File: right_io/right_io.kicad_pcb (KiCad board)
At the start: 8 copper layers, 58 x 185 mm, 163 parts, among them J11 USB-C dual-role data/PD port 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, J12 USB-C source-only data port J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, J30 External HDMI-A from TCP0, J500 JXD1-1022NL recessed 1GbE RJ45, Q2002 2N7002K DFP USB2 enable inver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, Q50 BSS138 HDMI bias gate, U1760 TPS2553DDBVR 1.3A USB branch, U1761 TPS25810RVCR Type-C DFP contr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, U1763 TPD1S514-1YZR 5.9V VBUS OVP, U1765 TPD4E05U06 USB2/CC ESD, U2011 TPD4S201 CC and USB2 short-to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, U2012 CAT24C256 32KB private TPS257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, U2013 TS3USB30E DFP-qualified USB2 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, U2014 SN74LVC2G07 partial-power-dow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, U2015 TVS2200 22V USB VBUS surge cl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, U2016 SN74LVC1G08 DFP and attached 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, U42 TPS25751AD USB-PD DRP control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, U50 TPD13S523PWR HDMI control ESD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, U500 RTL8111H-CG-RH PCIe Gigabit E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, U501 D3V3XA4B10LP-7 four-channel 0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, U502 D3V3XA4B10LP-7 four-channel 0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, U51 PCA9306DCTR HDMI DDC level tr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, U53 SN74LVC1G17DBVR HDMI HPD buff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, U54 TPS22975NDSGR host-active SYS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, U55 TPS22975NDSGR host-active SYS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, U721 TPS26630RGER PD2 default-off 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, Y500 ECS-250-8-33-AGN-TR 25MHz 8pF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

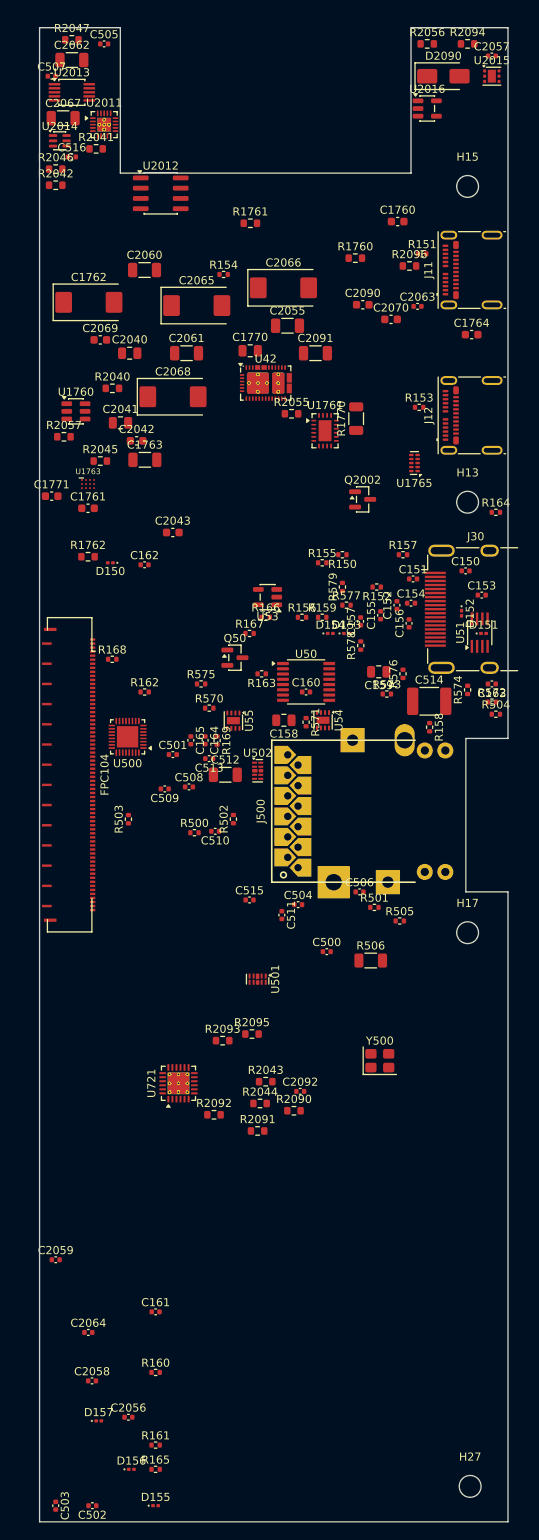
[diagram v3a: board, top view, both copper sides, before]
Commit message: Phase 5: second-opinion audit remediation + rebuilt, verified board pipeline
Second-opinion AI audit found A-tier defects; remediation applied and the
board pipeline rebuilt on a known-good base with the fixes it needed:

- electrical: LTC4418IUF symbol pinout corrected (both selectors were
  dead as drawn); center charge cascade (U15 <- U15B, PD1 > PD2 > AUX);
  pack negative never crosses FPC-3, 15-pin FG_VSS return; power-budgeted
  FPC pin maps (0.4 A/pin derate); J12/DS4 completed; AUX source fuse
- FH41-68S footprint: 13 datasheet-correct SH pads + SH pin in symbol
- connector geometry settled against the Hirose FH12 2D drawing: FFC
  enters opposite the solder pins (mouth = local +Y); reversed side-B
  maps are correct for the 180-deg-mounted pairs; rotations set so mouths
  face across every seam
- pipeline (generate_split_boards.py): per-pin pad-net resync from the
  netlists (kills shadow nets for good), netlist-exact name
  normalization, netlist-only part injection (cascade, probe headers),
  zone refill after outline swap, read-before-write race fixed, orphan
  parts dropped loudly, non-zero exit on unresolved overlaps
- monolith board relocated to old/monolith_ducktop2.kicad_pcb (placement
  oracle for the center cut only)

verified end state: 4 boards 0 shorts / 0 clearance / 0 drill, 0 boundary
crossings, 6/6 connectors contract-exact with mouths facing, 0 shadow
nets, gates PASS x4, ERC 0 x4. routing next (499 nets/board).
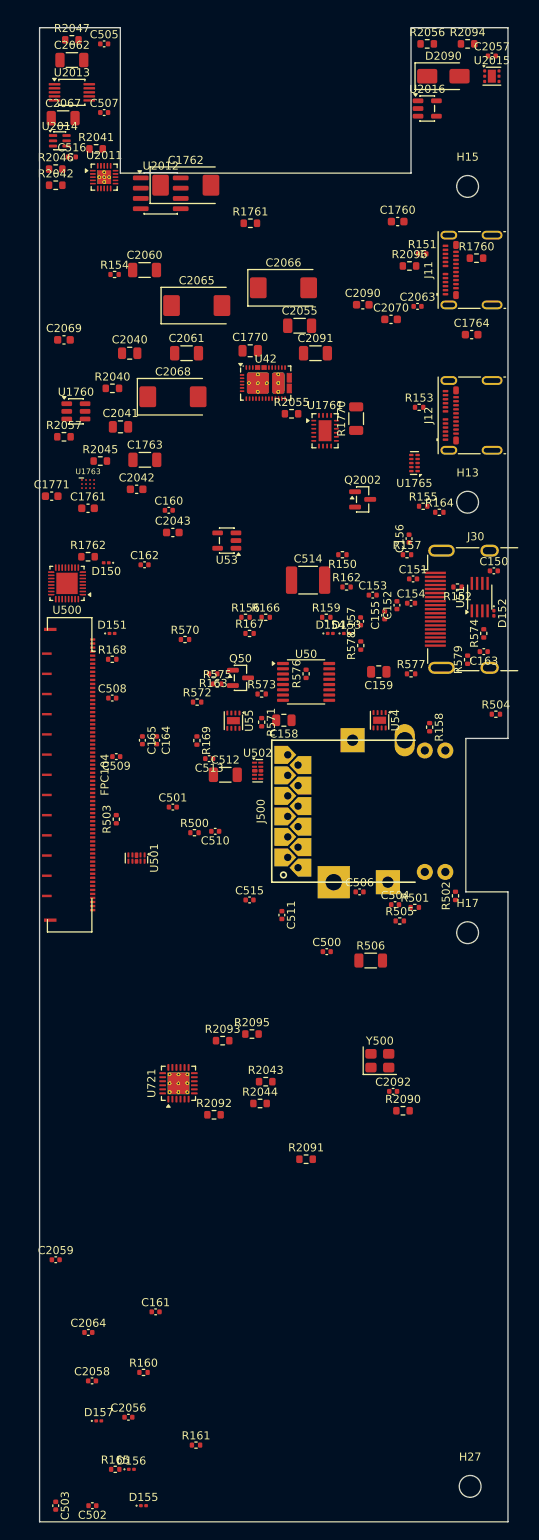
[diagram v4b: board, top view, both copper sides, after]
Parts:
- H13, H15, H17, H27: value MountingHole_2.7mm_M2.5 -> M2.5 isolated mainboard mounting hole
- moved D151 46.0 mm to (309.0, 75.0)
- moved R572 36.5 mm to (319.5, 83.5)
- moved R502 29.1 mm to (351.5, 107.5)
- moved C160 28.2 mm to (316.0, 59.8)
- moved R162 28.2 mm to (338.0, 69.2)
- moved C514 21.2 mm to (333.2, 68.4)
- moved U501 21.2 mm to (312.0, 102.8)
- moved U500 20.4 mm to (303.4, 68.8)
- moved C1762 18.8 mm to (318.1, 19.5)
- moved R579 17.9 mm to (353.0, 78.2)
- moved R573 15.5 mm to (327.5, 82.5)
- moved R1760 15.0 mm to (354.1, 28.5)
- moved C508 14.5 mm to (309.0, 83.0)
- moved R155 14.3 mm to (347.5, 59.2)
- moved C153 13.5 mm to (341.2, 70.2)
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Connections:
- net ETH_1V0 renamed /GbE/ETH_1V0
- net ETH_CHASSIS renamed /GbE/ETH_CHASSIS
- net ETH_CT renamed /GbE/ETH_CT
- net ETH_LED_1000_A renamed /GbE/ETH_LED_1000_A
- net ETH_LED_1000_N renamed /GbE/ETH_LED_1000_N
- net ETH_LED_ACT_A renamed /GbE/ETH_LED_ACT_A
- net ETH_LED_ACT_N renamed /GbE/ETH_LED_ACT_N
- net ETH_MDI0_N renamed /GbE/ETH_MDI0_N
- net ETH_MDI0_P renamed /GbE/ETH_MDI0_P
- net ETH_MDI1_N renamed /GbE/ETH_MDI1_N
- net ETH_MDI1_P renamed /GbE/ETH_MDI1_P
- net ETH_MDI2_N renamed /GbE/ETH_MDI2_N
- net ETH_MDI2_P renamed /GbE/ETH_MDI2_P
- net ETH_MDI3_N renamed /GbE/ETH_MDI3_N
- net ETH_MDI3_P renamed /GbE/ETH_MDI3_P
- net ETH_RSET renamed /GbE/ETH_RSET
- net ETH_XI renamed /GbE/ETH_XI
- net ETH_XO renamed /GbE/ETH_XO
- net EXT_HDMI_5V renamed /HDMI/EXT_HDMI_5V
- net EXT_HDMI_BIAS_GATE renamed /HDMI/EXT_HDMI_BIAS_GATE
- net EXT_HDMI_BIAS_RETURN renamed /HDMI/EXT_HDMI_BIAS_RETURN
- net EXT_HDMI_CK_N renamed /HDMI/EXT_HDMI_CK_N
- net EXT_HDMI_CK_P renamed /HDMI/EXT_HDMI_CK_P
- net EXT_HDMI_D0_N renamed /HDMI/EXT_HDMI_D0_N
- net EXT_HDMI_D0_P renamed /HDMI/EXT_HDMI_D0_P
- net EXT_HDMI_D1_N renamed /HDMI/EXT_HDMI_D1_N
- net EXT_HDMI_D1_P renamed /HDMI/EXT_HDMI_D1_P
- net EXT_HDMI_D2_N renamed /HDMI/EXT_HDMI_D2_N
- net EXT_HDMI_D2_P renamed /HDMI/EXT_HDMI_D2_P
- net EXT_HDMI_HPD_CONN renamed /HDMI/EXT_HDMI_HPD_CONN
- net EXT_HDMI_HPD_NODE renamed /HDMI/EXT_HDMI_HPD_NODE
- net EXT_HDMI_SCL_CONN renamed /HDMI/EXT_HDMI_SCL_CONN
- net EXT_HDMI_SDA_CONN renamed /HDMI/EXT_HDMI_SDA_CONN
- net GBE_HSI_N renamed /GbE/GBE_HSI_N
- net GBE_HSI_P renamed /GbE/GBE_HSI_P
- net GBE_HSO_N renamed /GbE/GBE_HSO_N
- net GBE_HSO_P renamed /GbE/GBE_HSO_P
- net GBE_ISOLATE_N renamed /GbE/GBE_ISOLATE_N
- net HDMI_3V3_SWITCH_CT renamed /HDMI/HDMI_3V3_SWITCH_CT
- net HDMI_5V_SWITCH_CT renamed /HDMI/HDMI_5V_SWITCH_CT
- net HDMI_DDC_REF5 renamed /HDMI/HDMI_DDC_REF5
- net HDMI_HOST_3V3 renamed /HDMI/HDMI_HOST_3V3
- net HDMI_SOURCE_5V renamed /HDMI/HDMI_SOURCE_5V
- net HDMI_TPD_D0_UNUSED renamed /HDMI/HDMI_TPD_D0_UNUSED
- net HDMI_TPD_D1_UNUSED renamed /HDMI/HDMI_TPD_D1_UNUSED
- net HDMI_TPD_D2_UNUSED renamed /HDMI/HDMI_TPD_D2_UNUSED
- net HDMI_TPD_D3_UNUSED renamed /HDMI/HDMI_TPD_D3_UNUSED
- net HDMI_TPD_D4_UNUSED renamed /HDMI/HDMI_TPD_D4_UNUSED
- net HDMI_TPD_D5_UNUSED renamed /HDMI/HDMI_TPD_D5_UNUSED
- net HDMI_TPD_D6_UNUSED renamed /HDMI/HDMI_TPD_D6_UNUSED
- net HDMI_TPD_D7_UNUSED renamed /HDMI/HDMI_TPD_D7_UNUSED
- net HDMI_TPD_D8_UNUSED renamed /HDMI/HDMI_TPD_D8_UNUSED
- net HDMI_TPD_D9_UNUSED renamed /HDMI/HDMI_TPD_D9_UNUSED
- net J12_5V_PRE renamed /PD2 Dual-Role/J12_5V_PRE
- net J12_CC1 renamed /PD2 Dual-Role/J12_CC1
- net J12_CC2 renamed /PD2 Dual-Role/J12_CC2
- net J12_ILIM renamed /PD2 Dual-Role/J12_ILIM
- net J12_POL_N renamed /PD2 Dual-Role/J12_POL_N
- net J12_REF renamed /PD2 Dual-Role/J12_REF
- net J12_REF_RTN renamed /PD2 Dual-Role/J12_REF_RTN
- net J12_VBUS renamed /PD2 Dual-Role/J12_VBUS
- net J12_VBUS_POWER renamed /PD2 Dual-Role/J12_VBUS_POWER
- net J12_VBUS_SYS renamed /PD2 Dual-Role/J12_VBUS_SYS
- net PD2_CC1_CONN renamed /PD2 Dual-Role/PD2_CC1_CONN
- net PD2_CC1_SYS renamed /PD2 Dual-Role/PD2_CC1_SYS
- net PD2_CC2_CONN renamed /PD2 Dual-Role/PD2_CC2_CONN
- net PD2_CC2_SYS renamed /PD2 Dual-Role/PD2_CC2_SYS
- net PD2_CC_ESD_VBIAS renamed /PD2 Dual-Role/PD2_CC_ESD_VBIAS
- net PD2_CC_FAULT_LOCAL_N renamed /PD2 Dual-Role/PD2_CC_FAULT_LOCAL_N
- net PD2_DM_CONN renamed /PD2 Dual-Role/PD2_DM_CONN
- net PD2_DM_HOST_SWITCHED renamed /PD2 Dual-Role/PD2_DM_HOST_SWITCHED
- net PD2_DP_CONN renamed /PD2 Dual-Role/PD2_DP_CONN
- net PD2_DP_HOST_SWITCHED renamed /PD2 Dual-Role/PD2_DP_HOST_SWITCHED
- net PD2_DRAIN_THERMAL renamed /PD2 Dual-Role/PD2_DRAIN_THERMAL
- net PD2_EEPROM_IRQ_N renamed /PD2 Dual-Role/PD2_EEPROM_IRQ_N
- net PD2_EEPROM_SCL renamed /PD2 Dual-Role/PD2_EEPROM_SCL
- net PD2_EEPROM_SDA renamed /PD2 Dual-Role/PD2_EEPROM_SDA
- net PD2_EFUSE_DVDT renamed /PD2 Dual-Role/PD2_EFUSE_DVDT
- net PD2_EFUSE_ILIM renamed /PD2 Dual-Role/PD2_EFUSE_ILIM
- net PD2_EFUSE_OV renamed /PD2 Dual-Role/PD2_EFUSE_OV
- net PD2_EFUSE_SHDN renamed /PD2 Dual-Role/PD2_EFUSE_SHDN
- net PD2_EFUSE_UV renamed /PD2 Dual-Role/PD2_EFUSE_UV
- net PD2_GPIO_ATTACH renamed /PD2 Dual-Role/PD2_GPIO_ATTACH
- net PD2_GPIO_DFP renamed /PD2 Dual-Role/PD2_GPIO_DFP
- net PD2_GPIO_FLIP renamed /PD2 Dual-Role/PD2_GPIO_FLIP
- net PD2_HOST_ATTACHED renamed /PD2 Dual-Role/PD2_HOST_ATTACHED
- net PD2_LDO1V5 renamed /PD2 Dual-Role/PD2_LDO1V5
- net PD2_LDO3V3 renamed /PD2 Dual-Role/PD2_LDO3V3
- net PD2_MUX_EN renamed /PD2 Dual-Role/PD2_MUX_EN
- net PD2_MUX_FLIP renamed /PD2 Dual-Role/PD2_MUX_FLIP
- net PD2_PPHV renamed /PD2 Dual-Role/PD2_PPHV
- net PD2_USB2_OE_N renamed /PD2 Dual-Role/PD2_USB2_OE_N
- C150 pad 1: TCP0_TX0_P -> /TCP0_TX0_P
- C151 pad 1: TCP0_TX0_N -> /TCP0_TX0_N
- C152 pad 1: TCP0_TXRX0_P -> /TCP0_TXRX0_P
- C153 pad 1: TCP0_TXRX0_N -> /TCP0_TXRX0_N
- C154 pad 1: TCP0_TX1_P -> /TCP0_TX1_P
- C155 pad 1: TCP0_TX1_N -> /TCP0_TX1_N
- C156 pad 1: TCP0_TXRX1_P -> /TCP0_TXRX1_P
- C157 pad 1: TCP0_TXRX1_N -> /TCP0_TXRX1_N
- C1760 pad 1: USB_PORT_5V -> /USB_PORT_5V
- C1764 pad 1: SYS_3V3 -> /SYS_3V3
- C2043 pad 1: SYS_3V3 -> /SYS_3V3
- C2055 pad 1: PD2_VBUS_RAW -> /PD2_VBUS_RAW
- C2056 pad 1: PD2_VBUS_RAW -> /PD2_VBUS_RAW
- C2057 pad 1: PD2_VBUS_RAW -> /PD2_VBUS_RAW
- C2058 pad 1: PD2_VBUS_RAW -> /PD2_VBUS_RAW
- C2059 pad 1: PD2_VBUS_RAW -> /PD2_VBUS_RAW
- C2062 pad 1: MCU_3V3 -> /MCU_3V3
- C2065 pad 1: USB_PORT_5V -> /USB_PORT_5V
- C2066 pad 1: USB_PORT_5V -> /USB_PORT_5V
- C2067 pad 1: USB_PORT_5V -> /USB_PORT_5V
- C2070 pad 1: SYS_3V3 -> /SYS_3V3
- C2091 pad 1: PD2_VBUS_GATED -> /PD2_VBUS_GATED
- C500 pad 1: GBE_HOST_TX_P -> /GBE_HOST_TX_P
- C501 pad 1: GBE_HOST_TX_N -> /GBE_HOST_TX_N
- C502 pad 2: GBE_HOST_RX_P -> /GBE_HOST_RX_P
- C503 pad 2: GBE_HOST_RX_N -> /GBE_HOST_RX_N
- C504 pad 1: PCIE_3V3 -> /PCIE_3V3
- C505 pad 1: PCIE_3V3 -> /PCIE_3V3
- C506 pad 1: PCIE_3V3 -> /PCIE_3V3
- D2090 pad 1: PD2_VBUS_GATED -> /PD2_VBUS_GATED
- FPC104 pad 1: SYS_5V -> /SYS_5V
- FPC104 pad 10: GND -> /PD2_VBUS_GATED
- FPC104 pad 11: MCU_3V3 -> /PD2_VBUS_GATED
- FPC104 pad 12: GND -> /PD2_VBUS_GATED
- FPC104 pad 13: PD2_VBUS_RAW -> /PD2_VBUS_GATED
- FPC104 pad 14: GND -> /PD2_VBUS_RAW
- FPC104 pad 15: MU_HOST_ACTIVE -> /PD2_VBUS_RAW
- FPC104 pad 16: GND -> /USB_PORT_5V
- FPC104 pad 17: PLTRST_SRC_N -> /USB_PORT_5V
- FPC104 pad 18: GND -> /USB_PORT_5V
- FPC104 pad 19: PCIE_WAKE_N -> /USB_PORT_5V
- FPC104 pad 2: SYS_5V -> /SYS_5V
- FPC104 pad 21: GBE_CLKREQ_N -> GND
- FPC104 pad 22: GND -> /SYS_3V3
- FPC104 pad 23: PD2_I2C_SCL -> /SYS_3V3
- FPC104 pad 24: PD2_I2C_SDA -> /PCIE_3V3
- FPC104 pad 25: GND -> /PCIE_3V3
- FPC104 pad 26: PD2_TCPC_IRQ_N -> /MCU_3V3
- FPC104 pad 27: GND -> /MCU_3V3
- FPC104 pad 28: PD2_PATH_EN -> GND
- FPC104 pad 29: GND -> /HUB_DS4_DP
- FPC104 pad 3: GND -> /SYS_5V
- FPC104 pad 30: PD2_EFUSE_FAULT_N -> /HUB_DS4_DM
- FPC104 pad 31: GND -> /HUB_PRT_CTL4
- FPC104 pad 32: PD_PROTECT_FAULT_N -> /MU_HOST_ACTIVE
- FPC104 pad 33: GND -> /PLTRST_SRC_N
- FPC104 pad 34: HUB_DS1_DP -> /PCIE_WAKE_N
- FPC104 pad 35: HUB_DS1_DM -> /GBE_CLKREQ_N
- FPC104 pad 36: GND -> /PD2_I2C_SCL
- FPC104 pad 37: TCP0_DDC_SCL -> /PD2_I2C_SDA
- FPC104 pad 38: TCP0_DDC_SDA -> /PD2_TCPC_IRQ_N
- FPC104 pad 39: GND -> /PD2_PATH_EN
- FPC104 pad 4: USB_PORT_5V -> /SYS_5V
- FPC104 pad 40: TCP0_HPD -> /PD2_EFUSE_FAULT_N
- FPC104 pad 41: GND -> /PD_PROTECT_FAULT_N
- FPC104 pad 42: GBE_REFCLK_P -> GND
- FPC104 pad 43: GBE_REFCLK_N -> /HUB_DS1_DP
- FPC104 pad 44: GND -> /HUB_DS1_DM
- FPC104 pad 45: GBE_HOST_RX_P -> GND
- FPC104 pad 46: GBE_HOST_RX_N -> /TCP0_DDC_SCL
- FPC104 pad 47: GND -> /TCP0_DDC_SDA
- FPC104 pad 48: GBE_HOST_TX_P -> /TCP0_HPD
- FPC104 pad 49: GBE_HOST_TX_N -> GND
- FPC104 pad 5: USB_PORT_5V -> GND
- FPC104 pad 50: GND -> /GBE_REFCLK_P
- FPC104 pad 51: TCP0_TX0_P -> /GBE_REFCLK_N
- FPC104 pad 52: TCP0_TX0_N -> GND
- FPC104 pad 53: GND -> /GBE_HOST_RX_P
- FPC104 pad 54: TCP0_TX1_P -> /GBE_HOST_RX_N
- FPC104 pad 55: TCP0_TX1_N -> GND
- FPC104 pad 56: GND -> /GBE_HOST_TX_P
- FPC104 pad 57: TCP0_TXRX0_P -> /GBE_HOST_TX_N
- FPC104 pad 58: TCP0_TXRX0_N -> GND
- FPC104 pad 59: GND -> /TCP0_TX0_P
- FPC104 pad 60: TCP0_TXRX1_P -> /TCP0_TX0_N
- FPC104 pad 61: TCP0_TXRX1_N -> GND
- FPC104 pad 62: GND -> /TCP0_TX1_P
- FPC104 pad 63: GND -> /TCP0_TX1_N
- FPC104 pad 65: GND -> /TCP0_TXRX0_P
- FPC104 pad 66: GND -> /TCP0_TXRX0_N
- FPC104 pad 67: GND -> /TCP0_TXRX1_P
- FPC104 pad 68: GND -> /TCP0_TXRX1_N
- FPC104 pad 7: SYS_3V3 -> /PD2_VBUS_GATED
- FPC104 pad 8: GND -> /PD2_VBUS_GATED
- FPC104 pad 9: PCIE_3V3 -> /PD2_VBUS_GATED
- J11 pad A10: (no net) -> unconnected-(J11-RX2--PadA10)
- J11 pad A11: (no net) -> unconnected-(J11-RX2+-PadA11)
- J11 pad A2: (no net) -> unconnected-(J11-TX1+-PadA2)
- J11 pad A3: (no net) -> unconnected-(J11-TX1--PadA3)
- J11 pad A4: PD2_VBUS_RAW -> /PD2_VBUS_RAW
- J11 pad A8: (no net) -> unconnected-(J11-SBU1-PadA8)
- J11 pad A9: PD2_VBUS_RAW -> /PD2_VBUS_RAW
- J11 pad B10: (no net) -> unconnected-(J11-RX1--PadB10)
- J11 pad B11: (no net) -> unconnected-(J11-RX1+-PadB11)
- J11 pad B2: (no net) -> unconnected-(J11-TX2+-PadB2)
- J11 pad B3: (no net) -> unconnected-(J11-TX2--PadB3)
- J11 pad B4: PD2_VBUS_RAW -> /PD2_VBUS_RAW
- J11 pad B8: (no net) -> unconnected-(J11-SBU2-PadB8)
- J11 pad B9: PD2_VBUS_RAW -> /PD2_VBUS_RAW
- J12 pad A10: (no net) -> unconnected-(J12-RX2--PadA10)
- J12 pad A11: (no net) -> unconnected-(J12-RX2+-PadA11)
- J12 pad A2: (no net) -> unconnected-(J12-TX1+-PadA2)
- J12 pad A3: (no net) -> unconnected-(J12-TX1--PadA3)
- J12 pad A6: HUB_DS4_DP -> /HUB_DS4_DP
- J12 pad A7: HUB_DS4_DM -> /HUB_DS4_DM
- J12 pad A8: (no net) -> unconnected-(J12-SBU1-PadA8)
- J12 pad B10: (no net) -> unconnected-(J12-RX1--PadB10)
- J12 pad B11: (no net) -> unconnected-(J12-RX1+-PadB11)
- J12 pad B2: (no net) -> unconnected-(J12-TX2+-PadB2)
- J12 pad B3: (no net) -> unconnected-(J12-TX2--PadB3)
- J12 pad B6: HUB_DS4_DP -> /HUB_DS4_DP
- J12 pad B7: HUB_DS4_DM -> /HUB_DS4_DM
- J12 pad B8: (no net) -> unconnected-(J12-SBU2-PadB8)
- J30 pad 13: (no net) -> unconnected-(J30-CEC-Pad13)
- J30 pad 14: (no net) -> unconnected-(J30-UTILITY-Pad14)
- R158 pad 2: TCP0_DDC_SCL -> /TCP0_DDC_SCL
- R159 pad 2: TCP0_DDC_SDA -> /TCP0_DDC_SDA
- R165 pad 1: MU_HOST_ACTIVE -> /MU_HOST_ACTIVE
- R1761 pad 1: SYS_3V3 -> /SYS_3V3
- R2040 pad 1: MCU_3V3 -> /MCU_3V3
- R2040 pad 2: PD_PROTECT_FAULT_N -> /PD_PROTECT_FAULT_N
- R2043 pad 1: MCU_3V3 -> /MCU_3V3
- R2043 pad 2: PD2_I2C_SDA -> /PD2_I2C_SDA
- R2044 pad 1: MCU_3V3 -> /MCU_3V3
- R2044 pad 2: PD2_I2C_SCL -> /PD2_I2C_SCL
- R2045 pad 1: MCU_3V3 -> /MCU_3V3
- R2045 pad 2: PD2_TCPC_IRQ_N -> /PD2_TCPC_IRQ_N
- R2046 pad 1: SYS_3V3 -> /SYS_3V3
- R2047 pad 1: SYS_3V3 -> /SYS_3V3
- R2056 pad 1: SYS_3V3 -> /SYS_3V3
- R2057 pad 2: PD_PROTECT_FAULT_N -> /PD_PROTECT_FAULT_N
- R2095 pad 1: PD2_PATH_EN -> /PD2_PATH_EN
- R2096 pad 1: MCU_3V3 -> /MCU_3V3
- R2096 pad 2: PD2_EFUSE_FAULT_N -> /PD2_EFUSE_FAULT_N
- R502 pad 1: PCIE_3V3 -> /PCIE_3V3
- R503 pad 1: PCIE_3V3 -> /PCIE_3V3
- R503 pad 2: PCIE_WAKE_N -> /PCIE_WAKE_N
- R504 pad 1: PCIE_3V3 -> /PCIE_3V3
- R505 pad 1: PCIE_3V3 -> /PCIE_3V3
- U1760 pad 1: USB_PORT_5V -> /USB_PORT_5V
- U1760 pad 3: HUB_PRT_CTL4 -> /HUB_PRT_CTL4
- U1760 pad 4: HUB_PRT_CTL4 -> /HUB_PRT_CTL4
- U1761 pad 1: HUB_PRT_CTL4 -> /HUB_PRT_CTL4
- U1761 pad 16: (no net) -> unconnected-(U1761-~{DEBUG}-Pad16)
- U1761 pad 17: (no net) -> unconnected-(U1761-~{AUDIO}-Pad17)
- U1761 pad 19: (no net) -> unconnected-(U1761-~{UFP}-Pad19)
- U1761 pad 20: (no net) -> unconnected-(U1761-~{LD_DET}-Pad20)
- U1761 pad 5: SYS_3V3 -> /SYS_3V3
- U1761 pad 6: HUB_PRT_CTL4 -> /HUB_PRT_CTL4
- U1765 pad 1: HUB_DS4_DP -> /HUB_DS4_DP
- U1765 pad 10: (no net) -> unconnected-(U1765-NC-Pad10)
- U1765 pad 2: HUB_DS4_DM -> /HUB_DS4_DM
- U1765 pad 6: (no net) -> unconnected-(U1765-NC-Pad6)
- U1765 pad 7: (no net) -> unconnected-(U1765-NC-Pad7)
- U1765 pad 9: (no net) -> unconnected-(U1765-NC-Pad9)
- U2011 pad 16: (no net) -> unconnected-(U2011-NC-Pad16)
- U2011 pad 17: (no net) -> unconnected-(U2011-NC-Pad17)
- U2011 pad 19: (no net) -> unconnected-(U2011-NC-Pad19)
- U2011 pad 20: (no net) -> unconnected-(U2011-NC-Pad20)
- U2013 pad 10: SYS_3V3 -> /SYS_3V3
- U2013 pad 2: HUB_DS1_DP -> /HUB_DS1_DP
- U2013 pad 3: (no net) -> unconnected-(U2013-D2+-Pad3)
- U2013 pad 7: (no net) -> unconnected-(U2013-D2--Pad7)
- U2013 pad 8: HUB_DS1_DM -> /HUB_DS1_DM
- U2014 pad 5: SYS_3V3 -> /SYS_3V3
- U2015 pad 4: PD2_VBUS_RAW -> /PD2_VBUS_RAW
- U2015 pad 5: PD2_VBUS_RAW -> /PD2_VBUS_RAW
- U2015 pad 6: PD2_VBUS_RAW -> /PD2_VBUS_RAW
- U2016 pad 5: SYS_3V3 -> /SYS_3V3
- U42 pad 10: PD2_TCPC_IRQ_N -> /PD2_TCPC_IRQ_N
- U42 pad 23: PD2_VBUS_RAW -> /PD2_VBUS_RAW
- U42 pad 32: PD2_VBUS_RAW -> /PD2_VBUS_RAW
- U42 pad 34: USB_PORT_5V -> /USB_PORT_5V
- U42 pad 38: MCU_3V3 -> /MCU_3V3
- U42 pad 8: PD2_I2C_SDA -> /PD2_I2C_SDA
- U42 pad 9: PD2_I2C_SCL -> /PD2_I2C_SCL
- U500 pad 11: PCIE_3V3 -> /PCIE_3V3
- U500 pad 12: GBE_CLKREQ_N -> /GBE_CLKREQ_N
- U500 pad 15: GBE_REFCLK_P -> /GBE_REFCLK_P
- U500 pad 16: GBE_REFCLK_N -> /GBE_REFCLK_N
- U500 pad 19: PLTRST_SRC_N -> /PLTRST_SRC_N
- U500 pad 21: PCIE_WAKE_N -> /PCIE_WAKE_N
- U500 pad 23: PCIE_3V3 -> /PCIE_3V3
- U500 pad 27: (no net) -> unconnected-(U500-LED0-Pad27)
- U500 pad 32: PCIE_3V3 -> /PCIE_3V3
- U501 pad 10: (no net) -> unconnected-(U501-NC-Pad10)
- U501 pad 6: (no net) -> unconnected-(U501-NC-Pad6)
- U501 pad 7: (no net) -> unconnected-(U501-NC-Pad7)
- U501 pad 9: (no net) -> unconnected-(U501-NC-Pad9)
- U502 pad 10: (no net) -> unconnected-(U502-NC-Pad10)
- U502 pad 6: (no net) -> unconnected-(U502-NC-Pad6)
- U502 pad 7: (no net) -> unconnected-(U502-NC-Pad7)
- U502 pad 9: (no net) -> unconnected-(U502-NC-Pad9)
- U51 pad 3: TCP0_DDC_SCL -> /TCP0_DDC_SCL
- U51 pad 4: TCP0_DDC_SDA -> /TCP0_DDC_SDA
- U53 pad 1: (no net) -> unconnected-(U53-NC-Pad1)
- U53 pad 4: TCP0_HPD -> /TCP0_HPD
- U54 pad 1: SYS_5V -> /SYS_5V
- U54 pad 2: SYS_5V -> /SYS_5V
- U54 pad 3: MU_HOST_ACTIVE -> /MU_HOST_ACTIVE
- U54 pad 4: SYS_5V -> /SYS_5V
- U55 pad 1: SYS_3V3 -> /SYS_3V3
- U55 pad 2: SYS_3V3 -> /SYS_3V3
- U55 pad 3: MU_HOST_ACTIVE -> /MU_HOST_ACTIVE
- U55 pad 4: SYS_3V3 -> /SYS_3V3
- U721 pad 13: (no net) -> unconnected-(U721-IMON-Pad13)
- U721 pad 14: PD2_EFUSE_FAULT_N -> /PD2_EFUSE_FAULT_N
- U721 pad 16: (no net) -> unconnected-(U721-PGOOD-Pad16)
- U721 pad 17: PD2_VBUS_GATED -> /PD2_VBUS_GATED
- U721 pad 18: PD2_VBUS_GATED -> /PD2_VBUS_GATED
- U721 pad 19: (no net) -> unconnected-(U721-NC-Pad19)
- U721 pad 20: (no net) -> unconnected-(U721-NC-Pad20)
- U721 pad 21: (no net) -> unconnected-(U721-NC-Pad21)
- U721 pad 22: (no net) -> unconnected-(U721-NC-Pad22)
- U721 pad 23: (no net) -> unconnected-(U721-NC-Pad23)
- U721 pad 24: (no net) -> unconnected-(U721-NC-Pad24)
- U721 pad 3: (no net) -> unconnected-(U721-B_GATE-Pad3)
- U721 pad 4: (no net) -> unconnected-(U721-DRV-Pad4)

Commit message: get the main boards ready for routing
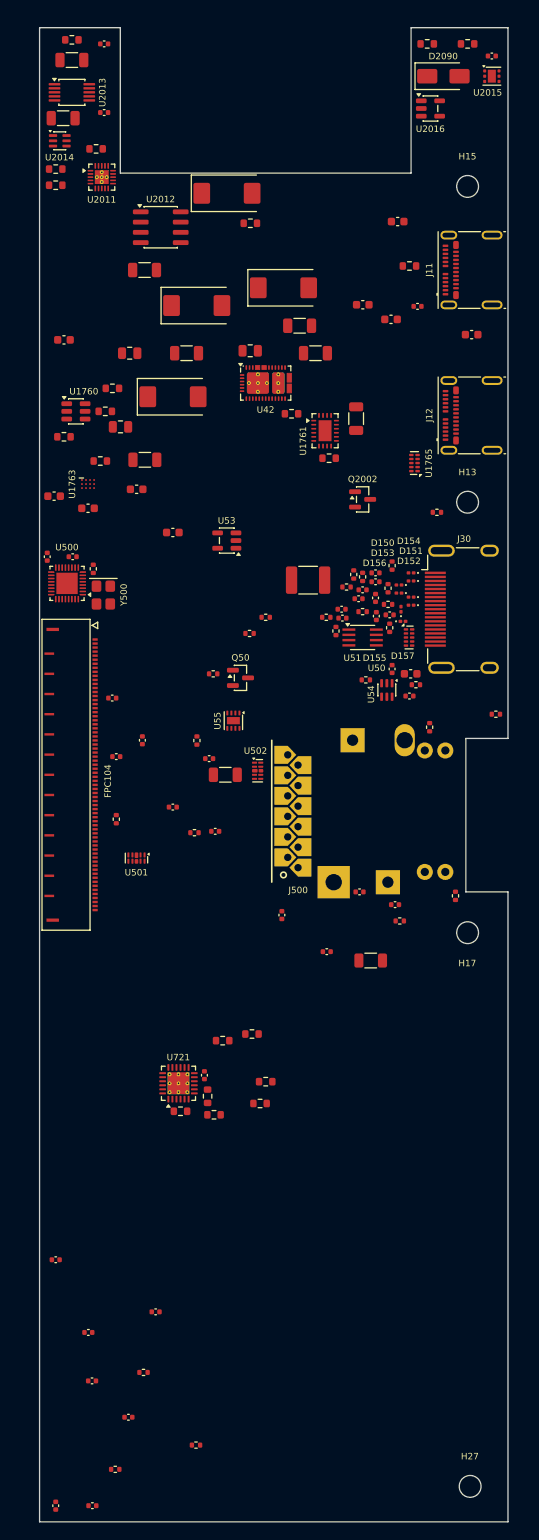
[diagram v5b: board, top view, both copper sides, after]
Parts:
- removed C159: 1u 10V X7R HDMI 5V switch output, Capacitor_SMD:C_0805_2012Metric
- removed C163: 100n 10V X7R HDMI 5V switch output HF, Capacitor_SMD:C_0402_1005Metric
- removed R571, R572, R573, R574, R575, R576, R577, R578, R579: 75R 1% unused TPD13S523 channel termination, Resistor_SMD:R_0402_1005Metric
- C158: value 1u 10V X7R HDMI 5V switch input -> 1u 10V X7R HDMI switch input; footprint Capacitor_SMD:C_0805_2012Metric -> Capacitor_SMD:C_0603_1608Metric
- C162: value 100n 10V X7R HDMI 5V switch input HF -> 100n 10V X7R HDMI switch input HF
- C164: value 4.7n HDMI 5V switch rise-time -> 18n 50V X7R TPS22948 output
- R570: value 75R 1% unused TPD13S523 channel termination -> 100k HDMI enable pulldown
- U50: value TPD13S523PWR HDMI control ESD / 5V switch -> TPD4E05U06DQAR HDMI control and 5V ESD; footprint Package_SO:TSSOP-16_4.4x5mm_P0.65mm -> Package_SON:USON-10_2.5x1.0mm_P0.5mm
- U54: value TPS22975NDSGR host-active SYS_5V switch -> TPS22948DCKR HDMI 5V current-limited switch; footprint Package_SON:Texas_DSG0008A_WSON-8-1EP_2x2mm_P0.5mm_EP0.9x1.6mm -> Package_TO_SOT_SMD:SOT-363_SC-70-6
- moved D155 116.3 mm to (346.0, 71.5), turned to 180 degrees
- moved D156 111.6 mm to (344.8, 72.0), turned to 90 degrees
- moved D157 105.9 mm to (345.0, 73.5)
- moved Y500 67.0 mm to (307.9, 70.2), turned to -90 degrees
- moved R501 57.8 mm to (306.6, 67.0), turned to 90 degrees
- moved R154 53.1 mm to (343.1, 71.4)
- moved R1760 49.7 mm to (308.1, 47.5)
- moved C516 49.5 mm to (304.1, 65.5)
- moved C515 49.3 mm to (300.9, 65.5), turned to 90 degrees
- moved R151 41.6 mm to (343.1, 69.4), turned to -90 degrees
- moved D150 37.8 mm to (346.0, 67.5)
- moved R168 37.7 mm to (346.6, 81.3)
- moved D151 37.6 mm to (346.0, 68.5), turned to 180 degrees
- moved C162 33.3 mm to (343.6, 79.4), turned to 90 degrees
- moved R1762 32.2 mm to (335.9, 53.3), turned to 180 degrees
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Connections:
- net /HUB_DS1_DM renamed /HUB_DS1_DN
- net /HUB_DS4_DM renamed /HUB_DS4_DN
- net /PD2 Dual-Role/PD2_DM_CONN renamed /PD2 Dual-Role/PD2_CONN_DN
- net /PD2 Dual-Role/PD2_DM_HOST_SWITCHED renamed /PD2 Dual-Role/PD2_HOST_SWITCHED_DN
- net /PD2 Dual-Role/PD2_DP_CONN renamed /PD2 Dual-Role/PD2_CONN_DP
- net /PD2 Dual-Role/PD2_DP_HOST_SWITCHED renamed /PD2 Dual-Role/PD2_HOST_SWITCHED_DP
- C158 pad 1: /HDMI/HDMI_SOURCE_5V -> /SYS_5V
- C162 pad 1: /HDMI/HDMI_SOURCE_5V -> /SYS_5V
- C164 pad 1: /HDMI/HDMI_5V_SWITCH_CT -> /HDMI/EXT_HDMI_5V
- R168 pad 1: /HDMI/HDMI_SOURCE_5V -> /HDMI/EXT_HDMI_5V
- R570 pad 1: /HDMI/HDMI_TPD_D0_UNUSED -> /MU_HOST_ACTIVE
- U50 pad 10: /HDMI/HDMI_TPD_D3_UNUSED -> unconnected-(U50-NC-Pad10)
- U50 pad 3: /HDMI/EXT_HDMI_HPD_CONN -> GND
- U50 pad 4: /HDMI/HDMI_TPD_D0_UNUSED -> /HDMI/EXT_HDMI_HPD_CONN
- U50 pad 5: /HDMI/HDMI_SOURCE_5V -> /HDMI/EXT_HDMI_5V
- U50 pad 6: /HDMI/EXT_HDMI_5V -> unconnected-(U50-NC-Pad6)
- U50 pad 7: /HDMI/HDMI_TPD_D1_UNUSED -> unconnected-(U50-NC-Pad7)
- U50 pad 9: /HDMI/HDMI_TPD_D2_UNUSED -> unconnected-(U50-NC-Pad9)
- U54 pad 2: /SYS_5V -> GND
- U54 pad 4: /SYS_5V -> unconnected-(U54-NC-Pad4)
- U54 pad 5: GND -> unconnected-(U54-~{FLT}-Pad5)
- U54 pad 6: /HDMI/HDMI_5V_SWITCH_CT -> /HDMI/EXT_HDMI_5V

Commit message: fix audit issues and move some connectors
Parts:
- removed H27: M2.5 isolated mainboard mounting hole, MountingHole:MountingHole_2.7mm_M2.5
- R2090: value 887k 0.1% 15V eFuse UV/OV top -> 8.87k 0.1% 10ppm 15/20V eFuse UV/OV top
- R2091: value 27.4k 0.1% 15V eFuse UV/OV middle -> 562R 0.1% 10ppm 15/20V eFuse UV/OV middle
- R2092: value 68.1k 0.1% 15V eFuse UV/OV bottom -> 511R 0.1% 10ppm 15/20V eFuse UV/OV bottom
- moved C2056 95.8 mm to (325.7, 77.4)
- moved C2058 95.8 mm to (321.2, 72.9)
- moved C2059 95.8 mm to (316.7, 57.9)
- moved C2064 95.8 mm to (320.7, 66.9)
- moved C161 95.8 mm to (329.0, 64.3)
- moved C502 95.8 mm to (321.2, 88.3)
- moved C503 95.8 mm to (316.7, 88.3)
- moved R160 95.8 mm to (327.5, 71.8)
- moved R161 95.8 mm to (334.0, 80.8)
- moved R165 95.8 mm to (324.0, 83.8)
- moved R2091 46.8 mm to (317.4, 85.6)
- moved R2093 46.8 mm to (319.2, 78.7)
- moved C2092 46.8 mm to (317.0, 83.0)
- moved R2092 46.8 mm to (318.1, 87.9)
- moved R2043 46.8 mm to (324.6, 83.8)
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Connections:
- J11 pad A10: unconnected-(J11-RX2--PadA10) -> (no net)
- J11 pad A11: unconnected-(J11-RX2+-PadA11) -> (no net)
- J11 pad A2: unconnected-(J11-TX1+-PadA2) -> (no net)
- J11 pad A3: unconnected-(J11-TX1--PadA3) -> (no net)
- J11 pad A8: unconnected-(J11-SBU1-PadA8) -> (no net)
- J11 pad B10: unconnected-(J11-RX1--PadB10) -> (no net)
- J11 pad B11: unconnected-(J11-RX1+-PadB11) -> (no net)
- J11 pad B2: unconnected-(J11-TX2+-PadB2) -> (no net)
- J11 pad B3: unconnected-(J11-TX2--PadB3) -> (no net)
- J11 pad B8: unconnected-(J11-SBU2-PadB8) -> (no net)
- J12 pad A10: unconnected-(J12-RX2--PadA10) -> (no net)
- J12 pad A11: unconnected-(J12-RX2+-PadA11) -> (no net)
- J12 pad A2: unconnected-(J12-TX1+-PadA2) -> (no net)
- J12 pad A3: unconnected-(J12-TX1--PadA3) -> (no net)
- J12 pad A8: unconnected-(J12-SBU1-PadA8) -> (no net)
- J12 pad B10: unconnected-(J12-RX1--PadB10) -> (no net)
- J12 pad B11: unconnected-(J12-RX1+-PadB11) -> (no net)
- J12 pad B2: unconnected-(J12-TX2+-PadB2) -> (no net)
- J12 pad B3: unconnected-(J12-TX2--PadB3) -> (no net)
- J12 pad B8: unconnected-(J12-SBU2-PadB8) -> (no net)
- J30 pad 13: unconnected-(J30-CEC-Pad13) -> (no net)
- J30 pad 14: unconnected-(J30-UTILITY-Pad14) -> (no net)
- U1761 pad 16: unconnected-(U1761-~{DEBUG}-Pad16) -> (no net)
- U1761 pad 17: unconnected-(U1761-~{AUDIO}-Pad17) -> (no net)
- U1761 pad 19: unconnected-(U1761-~{UFP}-Pad19) -> (no net)
- U1761 pad 20: unconnected-(U1761-~{LD_DET}-Pad20) -> (no net)
- U1765 pad 10: unconnected-(U1765-NC-Pad10) -> (no net)
- U1765 pad 6: unconnected-(U1765-NC-Pad6) -> (no net)
- U1765 pad 7: unconnected-(U1765-NC-Pad7) -> (no net)
- U1765 pad 9: unconnected-(U1765-NC-Pad9) -> (no net)
- U2011 pad 16: unconnected-(U2011-NC-Pad16) -> (no net)
- U2011 pad 17: unconnected-(U2011-NC-Pad17) -> (no net)
- U2011 pad 19: unconnected-(U2011-NC-Pad19) -> (no net)
- U2011 pad 20: unconnected-(U2011-NC-Pad20) -> (no net)
- U2013 pad 3: unconnected-(U2013-D2+-Pad3) -> (no net)
- U2013 pad 7: unconnected-(U2013-D2--Pad7) -> (no net)
- U50 pad 10: unconnected-(U50-NC-Pad10) -> (no net)
- U50 pad 6: unconnected-(U50-NC-Pad6) -> (no net)
- U50 pad 7: unconnected-(U50-NC-Pad7) -> (no net)
- U50 pad 9: unconnected-(U50-NC-Pad9) -> (no net)
- U500 pad 27: unconnected-(U500-LED0-Pad27) -> (no net)
- U501 pad 10: unconnected-(U501-NC-Pad10) -> (no net)
- U501 pad 6: unconnected-(U501-NC-Pad6) -> (no net)
- U501 pad 7: unconnected-(U501-NC-Pad7) -> (no net)
- U501 pad 9: unconnected-(U501-NC-Pad9) -> (no net)
- U502 pad 10: unconnected-(U502-NC-Pad10) -> (no net)
- U502 pad 6: unconnected-(U502-NC-Pad6) -> (no net)
- U502 pad 7: unconnected-(U502-NC-Pad7) -> (no net)
- U502 pad 9: unconnected-(U502-NC-Pad9) -> (no net)
- U53 pad 1: unconnected-(U53-NC-Pad1) -> (no net)
- U54 pad 4: unconnected-(U54-NC-Pad4) -> (no net)
- U54 pad 5: unconnected-(U54-~{FLT}-Pad5) -> (no net)
- U721 pad 13: unconnected-(U721-IMON-Pad13) -> (no net)
- U721 pad 16: unconnected-(U721-PGOOD-Pad16) -> (no net)
- U721 pad 19: unconnected-(U721-NC-Pad19) -> (no net)
- U721 pad 20: unconnected-(U721-NC-Pad20) -> (no net)
- U721 pad 21: unconnected-(U721-NC-Pad21) -> (no net)
- U721 pad 22: unconnected-(U721-NC-Pad22) -> (no net)
- U721 pad 23: unconnected-(U721-NC-Pad23) -> (no net)
- U721 pad 24: unconnected-(U721-NC-Pad24) -> (no net)
- U721 pad 3: unconnected-(U721-B_GATE-Pad3) -> (no net)
- U721 pad 4: unconnected-(U721-DRV-Pad4) -> (no net)
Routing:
- net /GbE/ETH_XI: track 0.00 -> 2.69 mm
- net /GbE/ETH_XO: track 0.00 -> 1.13 mm
- net GND: vias 0 -> 1
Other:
- board size 58 x 185 mm -> 58 x 117 mm

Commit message: fix more power stuff and update the left board
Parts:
- moved U2013 41.2 mm to (338.9, 30.1)
- moved U2011 39.4 mm to (345.4, 29.9), turned to 180 degrees
- moved C2061 31.5 mm to (344.6, 23.2)
- moved C162 30.2 mm to (313.8, 74.8)
- moved C158 30.2 mm to (316.1, 75.4)
- moved C164 30.2 mm to (316.0, 78.1)
- moved R168 30.2 mm to (316.8, 76.7)
- moved R570 30.2 mm to (310.6, 76.1)
- moved U54 30.2 mm to (313.2, 77.4)
- moved U42 23.4 mm to (338.9, 23.3), turned to 180 degrees
- moved R2096 19.0 mm to (330.4, 18.2)
- moved C165 14.1 mm to (326.8, 86.5), turned to 180 degrees
- moved C2090 13.1 mm to (333.9, 22.6), turned to 180 degrees
- moved R158 12.9 mm to (338.9, 77.8), turned to 180 degrees
- moved C2055 12.4 mm to (333.1, 24.6), turned to 180 degrees
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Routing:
- net GND: track 0.00 -> 76.3 mm, vias 1 -> 36
- net /PD2_VBUS_GATED: track 0.00 -> 25.0 mm
- net /HDMI/EXT_HDMI_SDA_CONN: track 0.00 -> 18.5 mm
- net /PD2 Dual-Role/PD2_CONN_DP: track 0.00 -> 13.7 mm
- net /HDMI/EXT_HDMI_BIAS_RETURN: track 0.00 -> 13.6 mm, vias 0 -> 5
- net /HDMI/HDMI_HOST_3V3: track 0.00 -> 12.0 mm
- net /PD2 Dual-Role/PD2_CC1_SYS: track 0.00 -> 11.4 mm
- net /HDMI/EXT_HDMI_CK_P: track 0.00 -> 11.4 mm, vias 0 -> 2
- net /HDMI/EXT_HDMI_5V: track 0.00 -> 9.75 mm, vias 0 -> 4
- net /HDMI/EXT_HDMI_CK_N: track 0.00 -> 9.54 mm, vias 0 -> 2
- net /HDMI/EXT_HDMI_SCL_CONN: track 0.00 -> 9.50 mm, vias 0 -> 1
- net /PD2 Dual-Role/PD2_CONN_DN: track 0.00 -> 9.23 mm
- net /HDMI/EXT_HDMI_D0_P: track 0.00 -> 8.74 mm
- net /PD2 Dual-Role/PD2_CC2_SYS: track 0.00 -> 8.73 mm
- net /HDMI/HDMI_DDC_REF5: track 0.00 -> 8.68 mm
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- added copper zone on B.Cu, net GND
- added copper zone on F.Cu, net GND
- added copper zone on In1.Cu, net GND
